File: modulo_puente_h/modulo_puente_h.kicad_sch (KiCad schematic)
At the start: 16 parts, among them J1 Conn_01x07_Pin, M1 Motor_IZQ, M2 Motor_DER, U1 L298N

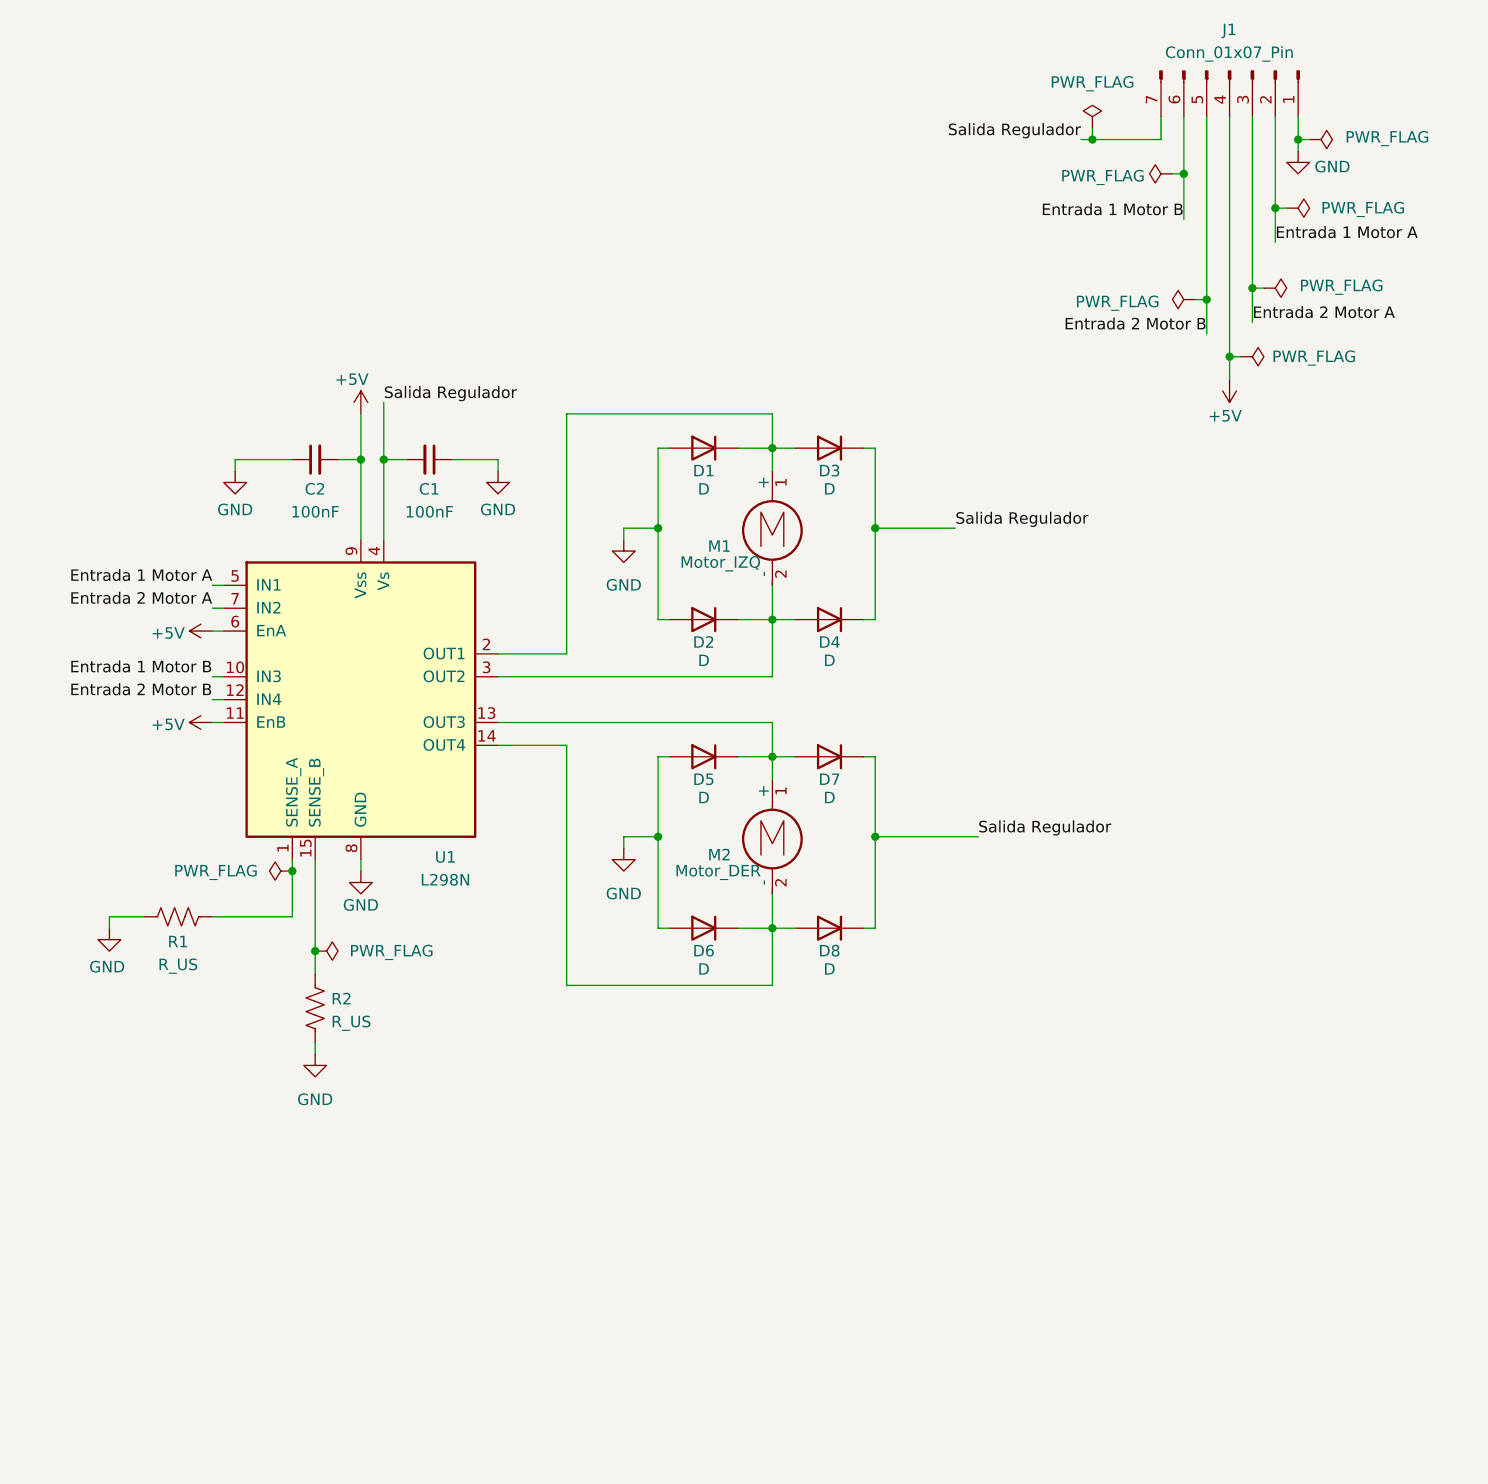
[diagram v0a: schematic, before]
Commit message: refactor!: Update de versión Kicad y corrijo nombres del esquemático
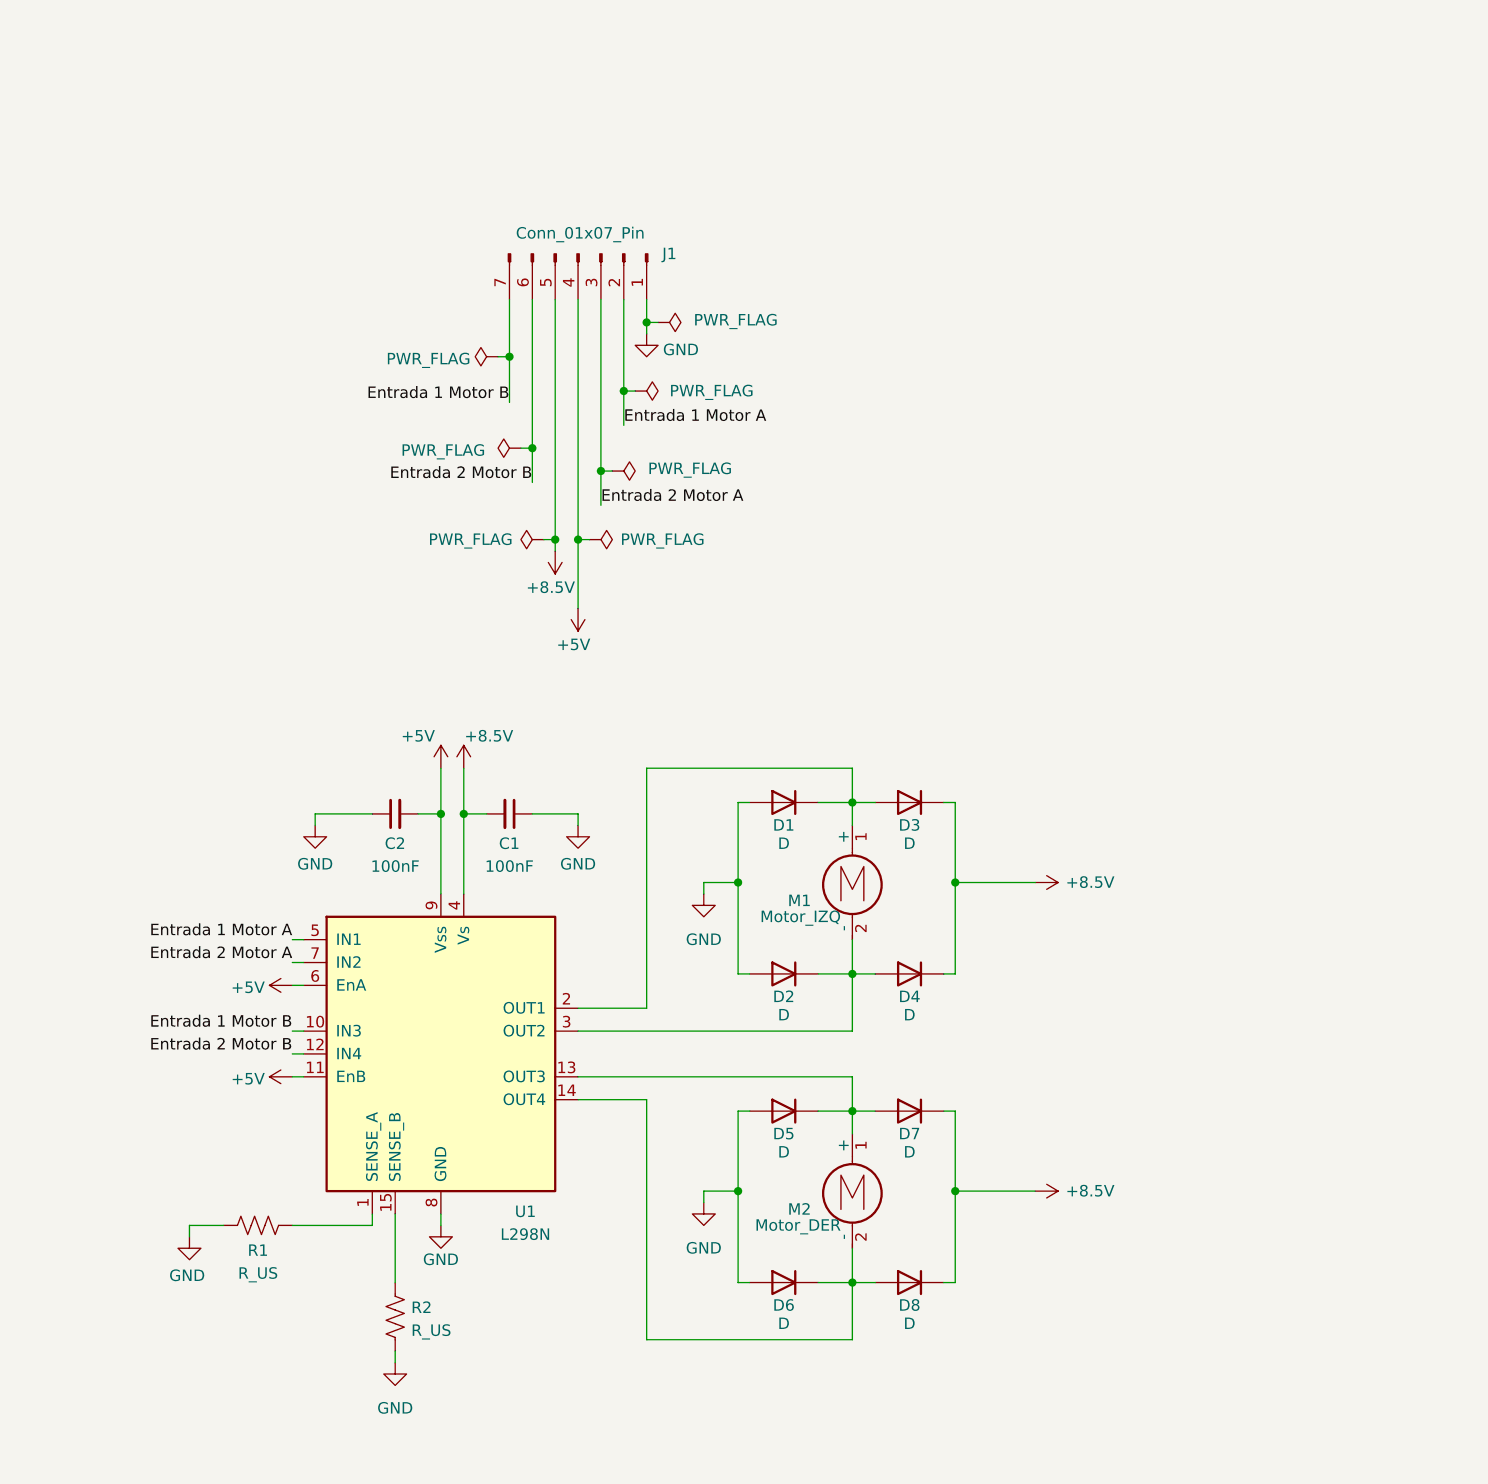
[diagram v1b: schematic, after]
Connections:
- net Entrada 1 Motor B: now also J1.7 (Pin_7); no longer J1.6 (Pin_6)
- net Entrada 2 Motor B: now also J1.6 (Pin_6); no longer J1.5 (Pin_5)
- net Salida Regulador renamed +8.5V
- net +8.5V: now also J1.5 (Pin_5); no longer J1.7 (Pin_7)
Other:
- moved on the sheet: C1, C2, D1, D2, D3, D4, D5, D6, D7, D8, J1, M1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

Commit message: fix: Agrego PWR_FLAGs para el ERC de Kicad y footprint del l298
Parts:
- U1: footprint Package_TO_SOT_THT:TO-220-15_P2.54x2.54mm_StaggerOdd_Lead4.58mm_Vertical -> Package_TO_SOT_THT:TO-220-15_P2.54x5.08mm_StaggerOdd_Lead4.58mm_Vertical
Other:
- moved on the sheet: R1, R2
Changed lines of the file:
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@@
 	)
 	(junction
+		(at 49.53 156.21)
+		(diameter 0)
+		(color 0 0 0 0)
+	)
+	(junction
 		(at 123.19 118.11)
 		(diameter 0)
@@
 	)
 	(junction
+		(at 60.96 166.37)
+		(diameter 0)
+		(color 0 0 0 0)
+	)
+	(junction
 		(at 111.76 109.22)
 		(diameter 0)
@@
 	(wire
 		(pts
-			(xy 58.42 156.21) (xy 49.53 156.21)
+			(xy 99.06 143.51) (xy 100.33 143.51)
 		)
 		(stroke
@@
 	(wire
 		(pts
-			(xy 99.06 143.51) (xy 100.33 143.51)
+			(xy 86.36 53.34) (xy 86.36 63.5)
 		)
 		(stroke
@@
 	(wire
 		(pts
-			(xy 86.36 53.34) (xy 86.36 63.5)
+			(xy 49.53 156.21) (xy 43.18 156.21)
 		)
 		(stroke
@@
 	(wire
 		(pts
+			(xy 60.96 154.94) (xy 60.96 166.37)
+		)
+		(stroke
+			(width 0)
+			(type default)
+		)
+	)
+	(wire
+		(pts
 			(xy 90.17 55.88) (xy 88.9 55.88)
 		)
@@
 	(wire
 		(pts
-			(xy 60.96 171.45) (xy 60.96 170.18)
+			(xy 60.96 176.53) (xy 60.96 175.26)
 		)
 		(stroke
@@
 	(wire
 		(pts
-			(xy 41.91 156.21) (xy 38.1 156.21)
+			(xy 35.56 156.21) (xy 31.75 156.21)
 		)
 		(stroke
@@
 	(wire
 		(pts
-			(xy 95.25 153.67) (xy 95.25 152.4)
+			(xy 60.96 167.64) (xy 60.96 166.37)
 		)
 		(stroke
@@
 	(wire
 		(pts
-			(xy 111.76 109.22) (xy 111.76 105.41)
+			(xy 95.25 153.67) (xy 95.25 152.4)
 		)
 		(stroke
@@
 	(wire
 		(pts
-			(xy 86.36 63.5) (xy 86.36 67.31)
+			(xy 111.76 109.22) (xy 111.76 105.41)
 		)
 		(stroke
@@
 	(wire
 		(pts
-			(xy 49.53 129.54) (xy 50.8 129.54)
+			(xy 86.36 63.5) (xy 86.36 67.31)
 		)
 		(stroke
@@
 	(wire
 		(pts
-			(xy 60.96 154.94) (xy 60.96 162.56)
+			(xy 49.53 129.54) (xy 50.8 129.54)
 		)
 		(stroke
@@
 	(wire
 		(pts
+			(xy 49.53 156.21) (xy 58.42 156.21)
+		)
+		(stroke
+			(width 0)
+			(type default)
+		)
+	)
+	(wire
+		(pts
 			(xy 111.76 134.62) (xy 111.76 128.27)
 		)
@@
 	(wire
 		(pts
-			(xy 38.1 156.21) (xy 38.1 157.48)
+			(xy 31.75 156.21) (xy 31.75 157.48)
 		)
 		(stroke
@@
 	(symbol
 		(lib_id "power:GNDS")
-		(at 38.1 157.48 0)
+		(at 31.75 157.48 0)
 		(unit 1)
 		(exclude_from_sim no)
@@
 		(dnp no)
 		(property "Reference" "#PWR015"
-			(at 38.1 163.83 0)
+			(at 31.75 163.83 0)
 			(effects
 				(font
@@
 		)
 		(property "Value" "GND"
-			(at 37.846 161.798 0)
+			(at 31.496 161.798 0)
 			(effects
 				(font
@@
 		)
 		(property "Footprint" ""
-			(at 38.1 157.48 0)
+			(at 31.75 157.48 0)
 			(effects
 				(font
@@
 		)
 		(property "Datasheet" ""
-			(at 38.1 157.48 0)
+			(at 31.75 157.48 0)
 			(effects
 				(font
@@
 		)
 		(property "Description" "Power symbol creates a global label with name \"GNDS\" , signal ground"
-			(at 38.1 157.48 0)
+			(at 31.75 157.48 0)
 			(effects
 				(font
@@
 	(symbol
 		(lib_id "power:GNDS")
-		(at 60.96 171.45 0)
+		(at 60.96 176.53 0)
 		(unit 1)
 		(exclude_from_sim no)
@@
 		(fields_autoplaced yes)
 		(property "Reference" "#PWR016"
-			(at 60.96 177.8 0)
+			(at 60.96 182.88 0)
 			(effects
 				(font
@@
 		)
 		(property "Value" "GND"
-			(at 60.96 176.53 0)
+			(at 60.96 181.61 0)
 			(effects
 				(font
@@
 		)
 		(property "Footprint" ""
-			(at 60.96 171.45 0)
+			(at 60.96 176.53 0)
 			(effects
 				(font
@@
 		)
 		(property "Datasheet" ""
-			(at 60.96 171.45 0)
+			(at 60.96 176.53 0)
 			(effects
 				(font
@@
 		)
 		(property "Description" "Power symbol creates a global label with name \"GNDS\" , signal ground"
-			(at 60.96 171.45 0)
+			(at 60.96 176.53 0)
 			(effects
 				(font
@@
 	(symbol
 		(lib_id "power:PWR_FLAG")
+		(at 49.53 156.21 180)
+		(unit 1)
+		(exclude_from_sim no)
+		(in_bom yes)
+		(on_board yes)
+		(dnp no)
+		(fields_autoplaced yes)
+		(property "Reference" "#FLG03"
+			(at 49.53 158.115 0)
+			(effects
+				(font
+					(size 1.27 1.27)
+				)
+				(hide yes)
+			)
+		)
+		(property "Value" "PWR_FLAG"
+			(at 49.53 161.29 0)
+			(effects
+				(font
+					(size 1.27 1.27)
+				)
+			)
+		)
+		(property "Footprint" ""
+			(at 49.53 156.21 0)
+			(effects
+				(font
+					(size 1.27 1.27)
+				)
+				(hide yes)
+			)
+		)
+		(property "Datasheet" "~"
+			(at 49.53 156.21 0)
+			(effects
+				(font
+					(size 1.27 1.27)
+				)
+				(hide yes)
+			)
+		)
+		(property "Description" "Special symbol for telling ERC where power comes from"
+			(at 49.53 156.21 0)
+			(effects
+				(font
+					(size 1.27 1.27)
+				)
+				(hide yes)
+			)
+		)
+		(pin "1"
+		)
+		(instances
+			(project ""
+				(path "/e8bedf4c-52de-4280-a6f9-25032b7792a2"
+					(reference "#FLG03")
+					(unit 1)
+				)
+			)
+		)
+	)
+	(symbol
+		(lib_id "power:PWR_FLAG")
 		(at 90.17 55.88 270)
 		(unit 1)
@@
 	(symbol
 		(lib_id "Device:R_US")
-		(at 60.96 166.37 180)
+		(at 60.96 171.45 180)
 		(unit 1)
 		(exclude_from_sim no)
@@
 		(dnp no)
 		(property "Reference" "R2"
-			(at 62.738 165.354 0)
+			(at 62.738 170.434 0)
 			(effects
 				(font
@@
 		)
 		(property "Value" "R_US"
-			(at 62.738 167.894 0)
+			(at 62.738 172.974 0)
 			(effects
 				(font
@@
 		)
 		(property "Footprint" "Resistor_SMD:R_0805_2012Metric_Pad1.20x1.40mm_HandSolder"
-			(at 59.944 166.116 90)
+			(at 59.944 171.196 90)
 			(effects
 				(font
@@
 		)
 		(property "Datasheet" "~"
-			(at 60.96 166.37 0)
+			(at 60.96 171.45 0)
 			(effects
 				(font
@@
 		)
 		(property "Description" "Resistor, US symbol"
-			(at 60.96 166.37 0)
+			(at 60.96 171.45 0)
 			(effects
 				(font
@@
 			)
 		)
-		(property "Footprint" "Package_TO_SOT_THT:TO-220-15_P2.54x2.54mm_StaggerOdd_Lead4.58mm_Vertical"
+		(property "Footprint" "Package_TO_SOT_THT:TO-220-15_P2.54x5.08mm_StaggerOdd_Lead4.58mm_Vertical"
 			(at 67.31 153.67 0)
 			(effects
@@
 	(symbol
 		(lib_id "Device:R_US")
-		(at 45.72 156.21 270)
+		(at 39.37 156.21 270)
 		(unit 1)
 		(exclude_from_sim no)
@@
 		(dnp no)
 		(property "Reference" "R1"
-			(at 45.72 159.004 90)
+			(at 39.37 159.004 90)
 			(effects
 				(font
@@
 		)
 		(property "Value" "R_US"
-			(at 45.72 161.544 90)
+			(at 39.37 161.544 90)
 			(effects
 				(font
@@
 		)
 		(property "Footprint" "Resistor_SMD:R_0805_2012Metric_Pad1.20x1.40mm_HandSolder"
-			(at 45.466 157.226 90)
+			(at 39.116 157.226 90)
 			(effects
 				(font
@@
 		)
 		(property "Datasheet" "~"
-			(at 45.72 156.21 0)
+			(at 39.37 156.21 0)
 			(effects
 				(font
@@
 		)
 		(property "Description" "Resistor, US symbol"
-			(at 45.72 156.21 0)
+			(at 39.37 156.21 0)
 			(effects
 				(font
@@
 					(unit 1)
 				)
+			)
+		)
+	)
+	(symbol
+		(lib_id "power:PWR_FLAG")
+		(at 60.96 166.37 270)
+		(unit 1)
+		(exclude_from_sim no)
+		(in_bom yes)
+		(on_board yes)
+		(dnp no)
+		(fields_autoplaced yes)
+		(property "Reference" "#FLG04"
+			(at 62.865 166.37 0)
+			(effects
+				(font
+					(size 1.27 1.27)
+				)
+				(hide yes)
+			)
+		)
+		(property "Value" "PWR_FLAG"
+			(at 64.77 166.3699 90)
+			(effects
+				(font
+					(size 1.27 1.27)
+				)
+				(justify left)
+			)
+		)
+		(property "Footprint" ""
+			(at 60.96 166.37 0)
+			(effects
+				(font
+					(size 1.27 1.27)
+				)
+				(hide yes)
+			)
+		)
+		(property "Datasheet" "~"
+			(at 60.96 166.37 0)
+			(effects
+				(font
+					(size 1.27 1.27)
+				)
+				(hide yes)
+			)
+		)
+		(property "Description" "Special symbol for telling ERC where power comes from"
+			(at 60.96 166.37 0)
+			(effects
+				(font
+					(size 1.27 1.27)
+				)
+				(hide yes)
+			)
+		)
+		(pin "1"
+		)
+		(instances
+			(project ""
+				(path "/e8bedf4c-52de-4280-a6f9-25032b7792a2"
+					(reference "#FLG04")
+					(unit 1)
+				)
